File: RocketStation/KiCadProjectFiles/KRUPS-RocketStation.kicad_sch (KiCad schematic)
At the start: 46 parts, among them J1 XT30U-M, J2 USB_C_Receptacle_USB2.0_16P, J3 RPi5_Header, J4 B2P-VH-FB-B, J5 B2P-VH-FB-B, J6 B2P-VH-FB-B, U1 PKU5511ESI, U2 AZ1117-3.3, U3 BME280, U4 SP3232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

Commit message: Small fixes for RocketStation v1
Modified RocketStation readme, fixed unconnected 3.3V test point, slightly changed async nets on schematic
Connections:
- net ASYNC_1: now also J6.2 (Pin_2), U4.7 (T2OUT); no longer J4.2 (Pin_2), U4.14 (T1OUT)
- net ASYNC_2: now also J4.2 (Pin_2), U4.14 (T1OUT); no longer J6.2 (Pin_2), U4.7 (T2OUT)
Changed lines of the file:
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@@
 	(text "Serial Data \nConnectors"
 		(exclude_from_sim no)
-		(at 209.55 150.622 0)
+		(at 214.884 150.368 0)
 		(effects
 			(font
@@
 		)
 	)
-	(label "ASYNC_1"
+	(label "ASYNC_2"
 		(at 177.8 151.13 0)
 		(fields_autoplaced yes)
@@
 		)
 	)
-	(label "ASYNC_2"
+	(label "ASYNC_1"
 		(at 177.8 160.02 0)
 		(fields_autoplaced yes)
@@
 		)
 	)
-	(label "ASYNC_2"
+	(label "ASYNC_1"
 		(at 217.17 118.11 180)
 		(fields_autoplaced yes)
@@
 		)
 	)
-	(label "ASYNC_1"
+	(label "ASYNC_2"
 		(at 217.17 113.03 180)
 		(fields_autoplaced yes)

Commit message: Added optional support for the LR62XE 1W radio
- Created a breakout/adapter board for the LR62XE 1W LoRa radio
- Modified the FemtoSat and RocketStation so that they'll be compatible with the adapter board
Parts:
- added TP2: TestPoint, TestPoint:TestPoint_Pad_2.0x2.0mm, symbol Connector:TestPoint
- added U8: LR62XE, KRUPS-FemtoSat:LR62XE, symbol KRUPS-FemtoSat:LR62XE
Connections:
- net +3V3: now also TP2.1, U8.5 (VDD_RADIO)
- net +5V: now also U8.11 (+5V)
- net GND: now also U8.10 (GND), U8.12 (GND)
- net LORA_BUSY: now also U8.3 (BUSY)
- net LORA_DIO1: now also U8.4 (DIO1)
- net LORA_TXEN: now also U8.1 (ANT-SW)
- net SPI_CLK: now also U8.6 (SCK)
- net SPI_MISO: now also U8.8 (MISO)
- net SPI_MOSI: now also U8.7 (MOSI)
- net SPI_NSS: now also U8.9 (NSS)
- net ~{LORA_RESET}: now also U8.2 (SX-NRESET)
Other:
- note added: "Alternate 1W LoRa Module 915MHz"
- note added: "LORA_TXEN goes to the RF Switch it switches between TX and RX modes Datasheet doesnt say if it needs to be high or low to enable TX, so idk"
- note added: "Only to be included if we can't use the Ebyte module Will be mounted via adapter board"
- note added: "TP2 is for LR62XE Power"

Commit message: Design Review Updates
Large number of design changes to both the FemtoSat (V5) and RocketStation (V3)

On both boards:
- Swapped the ESP32-S3-WROOM-2 modules to WROOM-1 modules due to supply issues
- Swapped power connectors to JST VH, data connectors to JST GH
- Added "Space Systems Lab, University of Kentucky, Lexington KY, USA, Earth" to the silkscreens
- Added test pads for IO pins, I2C bus, power
- Added LEDs connected to IO pins
- Changed power indication LEDs to a brighter LED
- Reformatted BOMs, they can now be generated by KiCad rather than being made by hand
- Updated documentation, 3D models

For Femtosat
- Removed 1 enclosure switch & MOSFET
- Moved a screw hole

and a bunch of other minor changes that I've forgotten
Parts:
- removed J4, J5, J6: B2P-VH-FB-B, KRUPS-RocketStation:JST_VH_B2P-VH-FB-B_1x02_P3.96mm_Vertical, symbol Connector_Generic:Conn_01x02
- added D1, D2: LED, Diode_SMD:D_0603_1608Metric_Pad1.05x0.95mm_HandSolder, symbol Device:LED
- added J4: Conn_02x02, Connector_PinHeader_2.54mm:PinHeader_2x02_P2.54mm_Vertical, symbol Connector_Generic:Conn_02x02_Top_Bottom
- added J5, J6, J7: BM02B-GHS-TBT, Connector_JST:JST_GH_BM02B-GHS-TBT_1x02-1MP_P1.25mm_Vertical, symbol Connector_Generic_MountingPin:Conn_01x02_MountingPin
- added R6, R7: 68, Resistor_SMD:R_0603_1608Metric_Pad0.98x0.95mm_HandSolder, symbol Device:R
- added TP3, TP4: TestPoint, Connector_PinHeader_2.54mm:PinHeader_1x01_P2.54mm_Vertical, symbol Connector:TestPoint
- C1, C10, C11, C12, C13, C14, C15, C16, C17, C19, C2: Digikey Part Number (none) -> CC0603KRX7R7BB104
- C18: Digikey Part Number (none) -> A768MS107M1JLAV027
- C3: Digikey Part Number (none) -> CL31A107MQHNNWE
- C4: Digikey Part Number (none) -> 12061C225KAT2A
- C5, C8, C9: Digikey Part Number (none) -> CL21A226MPQNNNE
- C6: Digikey Part Number (none) -> A768MS477M1ELAV017
- C7: Digikey Part Number (none) -> CL21A106KOQNNNG
- J1: value XT30U-M -> B2P-VH-FB-B; footprint Connector_AMASS:AMASS_XT30U-M_1x02_P5.0mm_Vertical -> Connector_JST:JST_VH_B2P-VH-FB-B_1x02_P3.96mm_Vertical; Digikey Part Number (none) -> B2P-VH-FB-B
- J2: Digikey Part Number (none) -> USB4110-GF-A
- J3: Digikey Part Number (none) -> PRT-16764
- R1, R2: Digikey Part Number (none) -> RC0603FR-075K1L
- R3, R4: Digikey Part Number (none) -> ERJ-3EKF3901V
- R5: Digikey Part Number (none) -> ERJ-3EKF2002V
- R8: renamed from R6; Digikey Part Number (none) -> ERJ-3EKF2002V
- R9: renamed from R7; Digikey Part Number (none) -> ERJ-3EKF2001V
- TP2: renamed from TP1; now left out of the parts list
- U1: Digikey Part Number (none) -> PKU5511ESI
- U2: Digikey Part Number (none) -> AZ1117CR2-3.3TRG1
- U3: Digikey Part Number (none) -> BME280
- U5: renamed from U4; Digikey Part Number (none) -> SP3232EUEY-L/TR
- U6: renamed from U5; value ESP32-S3-WROOM-2 -> ESP32-S3-WROOM-1-N16R8; Digikey Part Number (none) -> ESP32-S3-WROOM-1-N16R8
- U7: renamed from U6; Digikey Part Number (none) -> BNO086
- U8: renamed from U7; Digikey Part Number (none) -> ORDER SEPERATELY; now left out of the parts list
- renumbered TP2 to TP1, U8 to U4
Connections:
- net +3V3: now also R6.1
- net +5V: now also TP3.1
- net ASYNC_1: now also J7.2 (Pin_2)
- net ASYNC_2: now also J5.2 (Pin_2)
- net GND: now also D1.1 (K), D2.1 (K), J5.1 (Pin_1), J5.MP (MountPin), J6.MP (MountPin), J7.1 (Pin_1), J7.MP (MountPin), TP4.1
- net I2C_SCL: now also J4.1 (Pin_1)
- net I2C_SDA: now also J4.2 (Pin_2)
- net at R8.2: now also J6.1 (Pin_1)
- net IO38: now reaches U6.31 (IO38)
- net IO38: now also J4.4 (Pin_4)
- net IO39: now reaches U6.32 (MTCK/IO39)
- net IO39: now also J4.3 (Pin_3)
- net GPIO_LED: now reaches U6.33 (MTDO/IO40)
- net GPIO_LED: now also R7.1
- new net: D1.2 (A), R6.2
- new net: D2.2 (A), R7.2
- no-connect marks 52 -> 49
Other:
- note added: "ESP32-S3-WROOM-1 16MB Flash, 8MB PSRAM SoM"
- note added: "JST-GH"
- note added: "Red LED PN: APT1608SURCK Vf = 1.95V If = 20.0mA"
- note added: "WROOM-2 modules are currently out of stock so a WROOM-1 has been substituted. The only difference between the two is that the WROOM 2 has octal SPI flash/PSRAM. The WROOM-2 is otherwise pin compatible with this PCB."
- note added: "for LR62XE Power"
- note removed: "ESP32-S3-WROOM-2 32MB Flash, 8MB PSRAM SoM"
- note removed: "TP2 is for LR62XE Power"
- note removed: "Works with JST-VH cables/connectors"
- moved on the sheet: C3, C4, C5, C6, R8, R9, TP1, TP2, U1

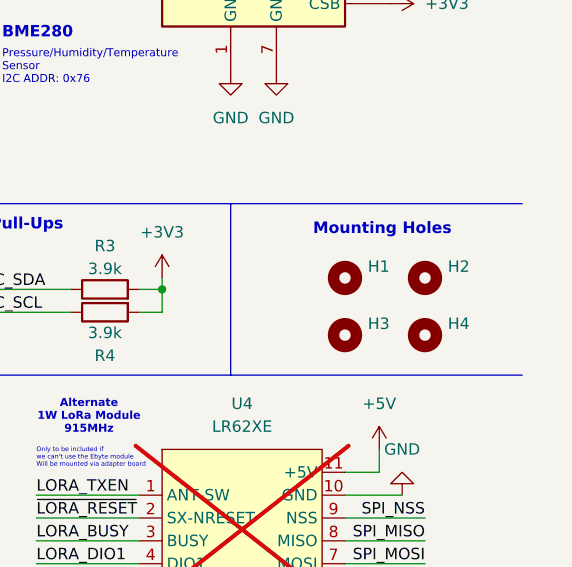
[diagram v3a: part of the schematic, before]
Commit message: Added fiducials to femtosat (v6) and rocketstation (v4)
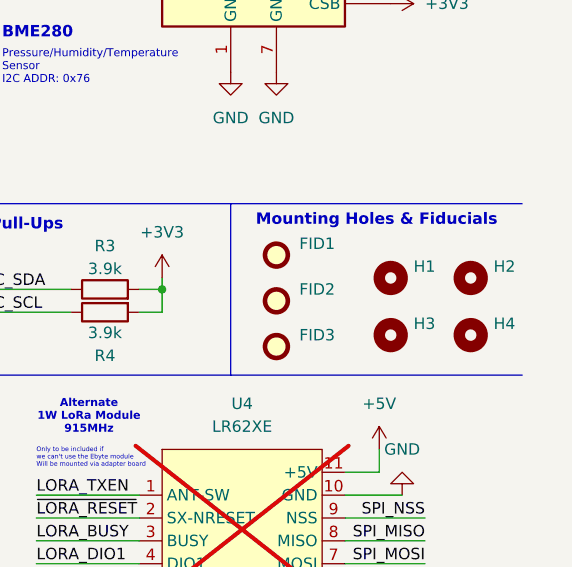
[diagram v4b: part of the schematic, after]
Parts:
- added FID1, FID2, FID3: Fiducial, Fiducial:Fiducial_0.75mm_Mask1.5mm, symbol Mechanical:Fiducial
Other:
- note added: "Mounting Holes & Fiducials"
- note removed: "Mounting Holes"
- moved on the sheet: H1, H2, H3, H4

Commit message: Corrected part numbers for C3 and C18 in BOM
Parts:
- C18: Digikey Part Number A768MS107M1JLAV027 -> CL31A107MQHNNNE
- C3: Digikey Part Number CL31A107MQHNNWE -> A768MS107M1JLAV027
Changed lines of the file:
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@@
 			)
 		)
-		(property "Digikey Part Number" "CL31A107MQHNNWE"
+		(property "Digikey Part Number" "A768MS107M1JLAV027"
 			(at 33.02 30.48 0)
 			(effects
@@
 			)
 		)
-		(property "Digikey Part Number" "A768MS107M1JLAV027"
+		(property "Digikey Part Number" "CL31A107MQHNNNE"
 			(at 19.05 166.37 0)
 			(effects

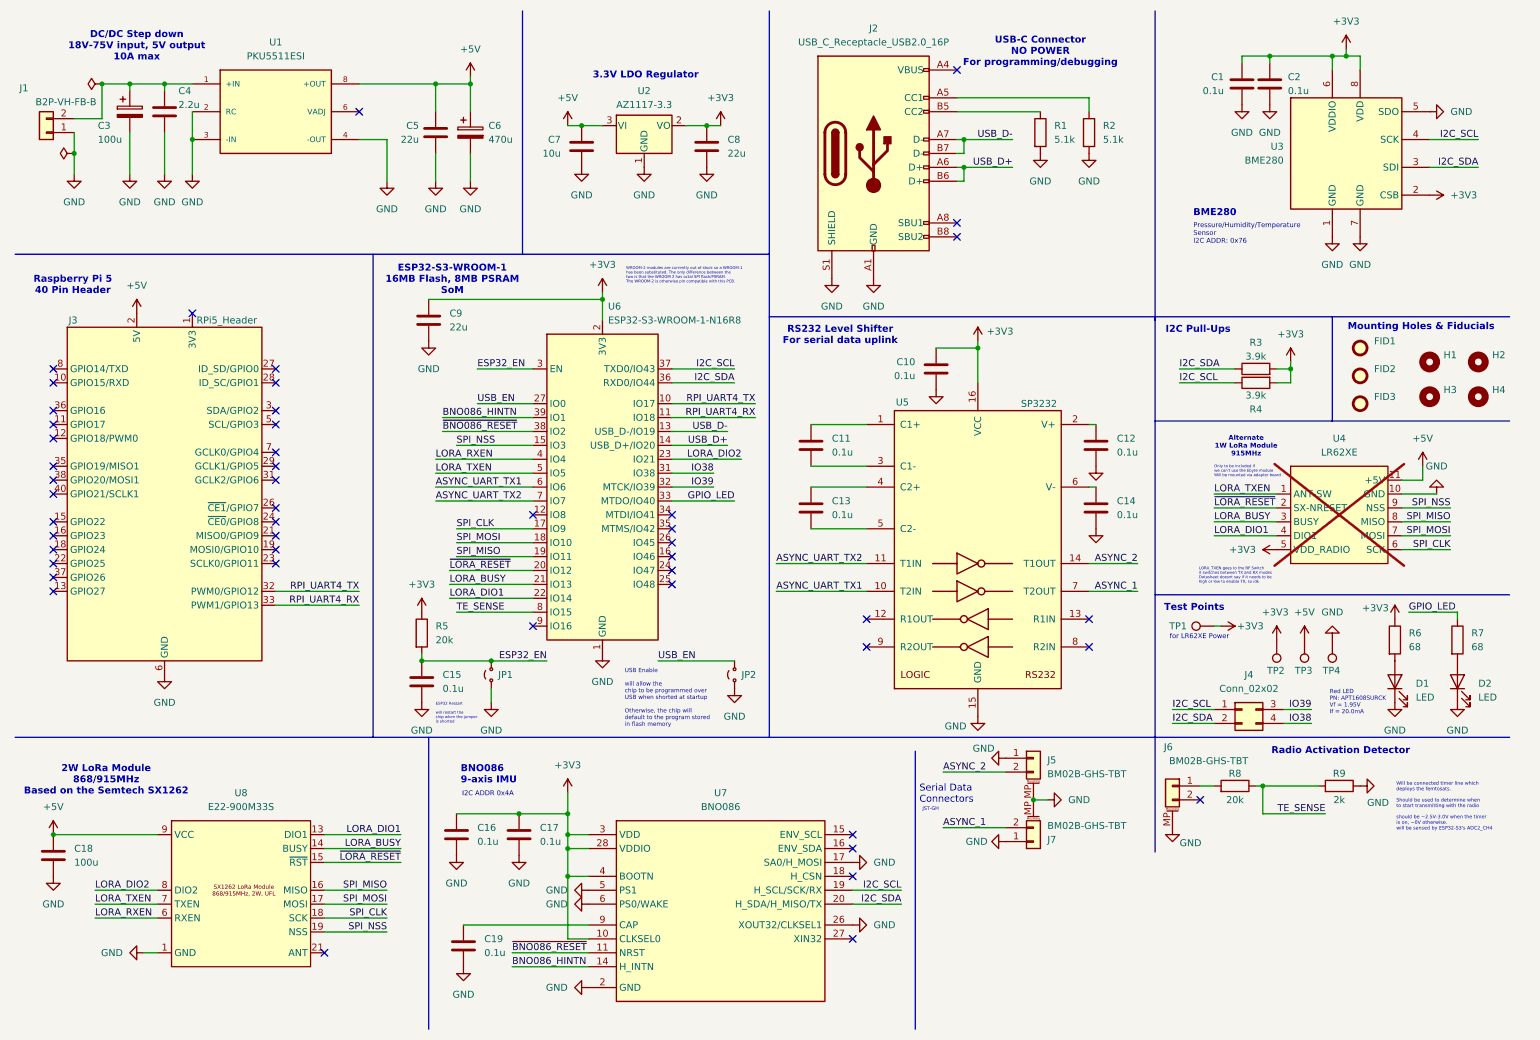
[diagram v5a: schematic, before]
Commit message: Changed to Raspi Pico, 1W radio
- Swapped the ESP32 S3 WROOM to a Raspberry Pi Pico 2 W on both the FemtoSat and RocketStation
- Swapped to 1W LoRa module in place of the 2W EBYTE one
- bunch of layout, documentation, miscellaneous changes
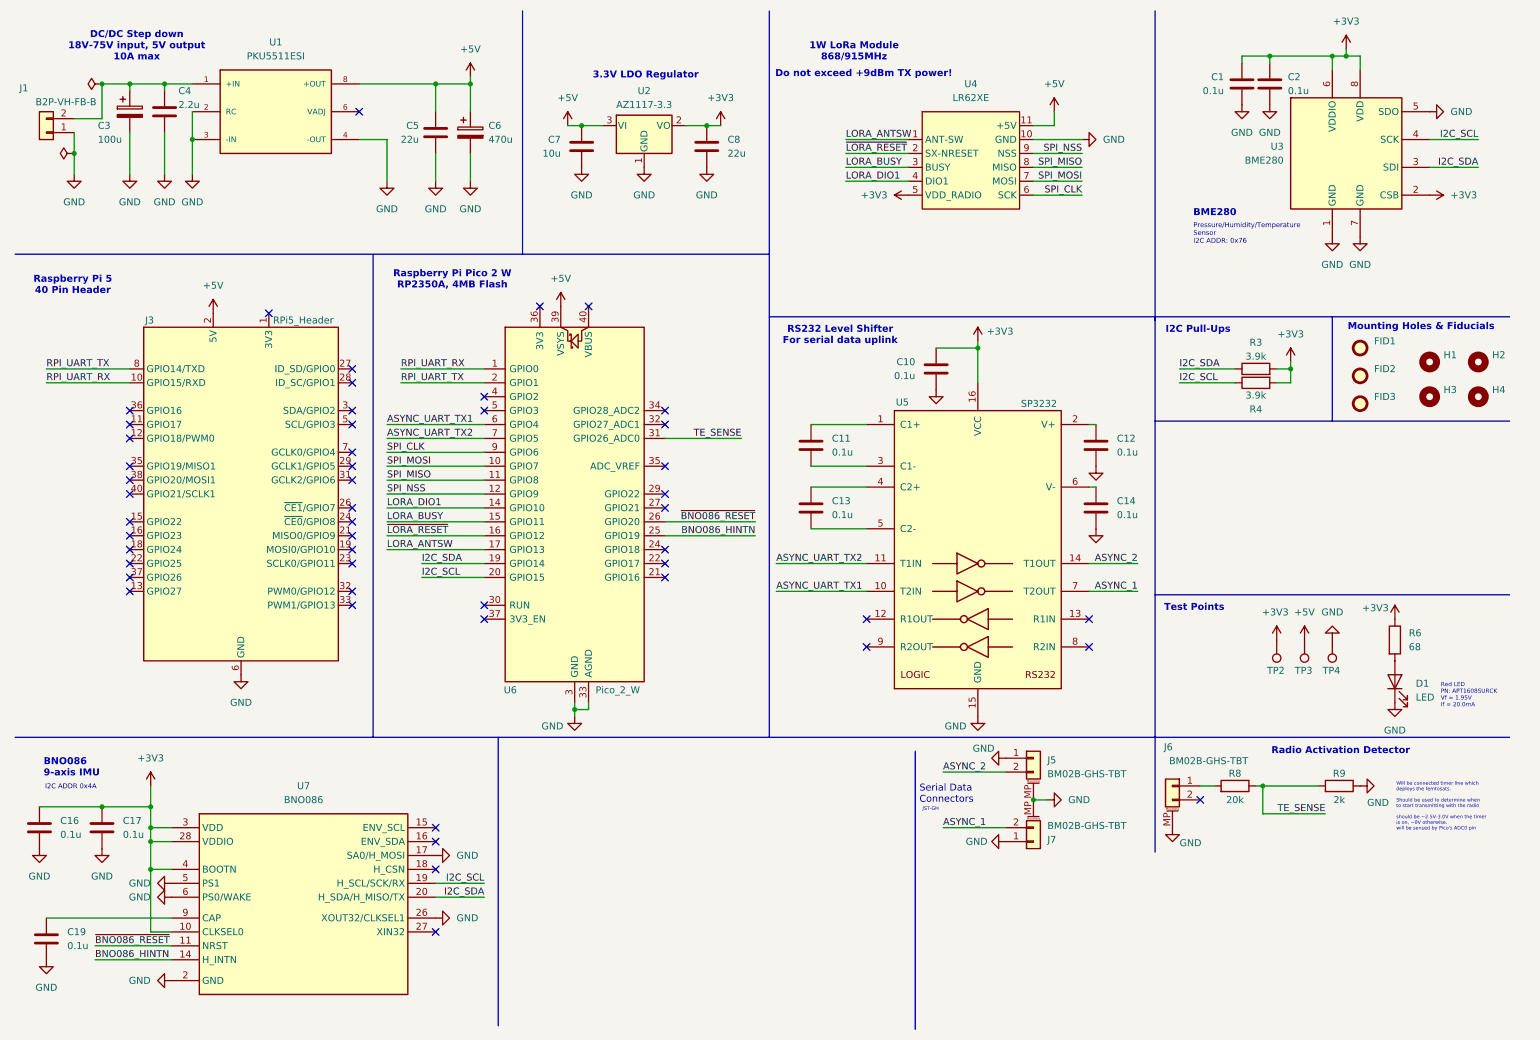
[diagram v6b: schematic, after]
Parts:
- removed C15: 0.1u, Capacitor_SMD:C_0603_1608Metric_Pad1.08x0.95mm_HandSolder, symbol Device:C
- removed C18: 100u, Capacitor_SMD:C_1206_3216Metric_Pad1.33x1.80mm_HandSolder, symbol Device:C
- removed C9: 22u, Capacitor_SMD:C_0805_2012Metric_Pad1.18x1.45mm_HandSolder, symbol Device:C
- removed D2: LED, Diode_SMD:D_0603_1608Metric_Pad1.05x0.95mm_HandSolder, symbol Device:LED
- removed J2: USB_C_Receptacle_USB2.0_16P, Connector_USB:USB_C_Receptacle_GCT_USB4110, symbol Connector:USB_C_Receptacle_USB2.0_16P
- removed J4: Conn_02x02, Connector_PinHeader_2.54mm:PinHeader_2x02_P2.54mm_Vertical, symbol Connector_Generic:Conn_02x02_Top_Bottom
- removed JP1, JP2: Jumper_2_Small_Open, TestPoint:TestPoint_2Pads_Pitch2.54mm_Drill0.8mm, symbol Jumper:Jumper_2_Small_Open
- removed R1, R2: 5.1k, Resistor_SMD:R_0603_1608Metric_Pad0.98x0.95mm_HandSolder, symbol Device:R
- removed R5: 20k, Resistor_SMD:R_0603_1608Metric_Pad0.98x0.95mm_HandSolder, symbol Device:R
- removed R7: 68, Resistor_SMD:R_0603_1608Metric_Pad0.98x0.95mm_HandSolder, symbol Device:R
- removed TP1: TestPoint, TestPoint:TestPoint_Pad_2.0x2.0mm, symbol Connector:TestPoint
- removed U6: ESP32-S3-WROOM-1-N16R8, RF_Module:ESP32-S3-WROOM-2, symbol RF_Module:ESP32-S3-WROOM-2
- removed U8: E22-900M33S, KRUPS-RocketStation:E22-XXXM33S, symbol KRUPS-RocketStation:E22-900M33S
- added U6: Pico_2_W, Module:RaspberryPi_Pico_Common_THT, symbol KRUPS-RocketStation:Pico_2_W
- U4: footprint KRUPS-FemtoSat:LR62XE -> KRUPS-RocketStation:LR62XE; now fitted
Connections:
- net +5V: now also U6.39 (VSYS)
- net ASYNC_UART_TX1: now also U6.6 (GPIO4)
- net ASYNC_UART_TX2: now also U6.7 (GPIO5)
- net BNO086_HINTN: now also U6.25 (GPIO19)
- net GND: now also U6.13 (GND), U6.18 (GND), U6.23 (GND), U6.28 (GND), U6.3 (GND), U6.33 (AGND), U6.38 (GND), U6.8 (GND)
- net I2C_SCL: now also U6.20 (GPIO15)
- net I2C_SDA: now also U6.19 (GPIO14)
- net LORA_BUSY: now also U6.15 (GPIO11)
- net LORA_DIO1: now also U6.14 (GPIO10)
- net SPI_CLK: now also U6.9 (GPIO6)
- net SPI_MISO: now also U6.11 (GPIO8)
- net SPI_MOSI: now also U6.10 (GPIO7)
- net SPI_NSS: now also U6.12 (GPIO9)
- net TE_SENSE: now also U6.31 (GPIO26_ADC0)
- net ~{BNO086_RESET}: now also U6.26 (GPIO20)
- net ~{LORA_RESET}: now also U6.16 (GPIO12)
- net RPI_UART_RX: now reaches J3.10 (GPIO15/RXD)
- net RPI_UART_RX: now also U6.1 (GPIO0)
- net RPI_UART_TX: now reaches J3.8 (GPIO14/TXD)
- net RPI_UART_TX: now also U6.2 (GPIO1)
- net LORA_TXEN renamed LORA_ANTSW
- net LORA_ANTSW: now also U6.17 (GPIO13)
- net RPI_UART4_RX: no longer names the net of J3.33 (PWM1/GPIO13)
- net RPI_UART4_TX: no longer names the net of J3.32 (PWM0/GPIO12)
- no-connect marks 49 -> 51
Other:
- note added: "1W LoRa Module 868/915MHz"
- note added: "Do not exceed +9dBm TX power!"
- note added: "Raspberry Pi Pico 2 W RP2350A, 4MB Flash"
- note added: "Will be connected timer line which deploys the femtosats. Should be used to determine when to start transmitting with the radio should be ~2.5V-3.0V when the timer is on, ~0V otherwise. will be sensed by Pico's ADC0 pin"
- note removed: "2W LoRa Module 868/915MHz Based on the Semtech SX1262"
- note removed: "Alternate 1W LoRa Module 915MHz"
- note removed: "ESP32 Restart will restart the chip when the jumper is shorted"
- note removed: "ESP32-S3-WROOM-1 16MB Flash, 8MB PSRAM SoM"
- note removed: "LORA_TXEN goes to the RF Switch it switches between TX and RX modes Datasheet doesnt say if it needs to be high or low to enable TX, so idk"
- note removed: "Only to be included if we can't use the Ebyte module Will be mounted via adapter board"
- note removed: "USB Enable will allow the chip to be programmed over USB when shorted at startup Otherwise, the chip will default to the program stored in flash memory"
- note removed: "USB-C Connector NO POWER For programming/debugging"
- note removed: "WROOM-2 modules are currently out of stock so a WROOM-1 has been substituted. The only difference between the two is that the WROOM 2 has octal SPI flash/PSRAM. The WROOM-2 is otherwise pin compatible with this PCB."
- note removed: "Will be connected timer line which deploys the femtosats. Should be used to determine when to start transmitting with the radio should be ~2.5V-3.0V when the timer is on, ~0V otherwise. will be sensed by ESP32-S3's ADC2_CH4"
- note removed: "for LR62XE Power"
- moved on the sheet: C16, C17, C19, J3, U7
